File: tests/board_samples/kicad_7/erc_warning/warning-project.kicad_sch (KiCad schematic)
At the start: 0 parts

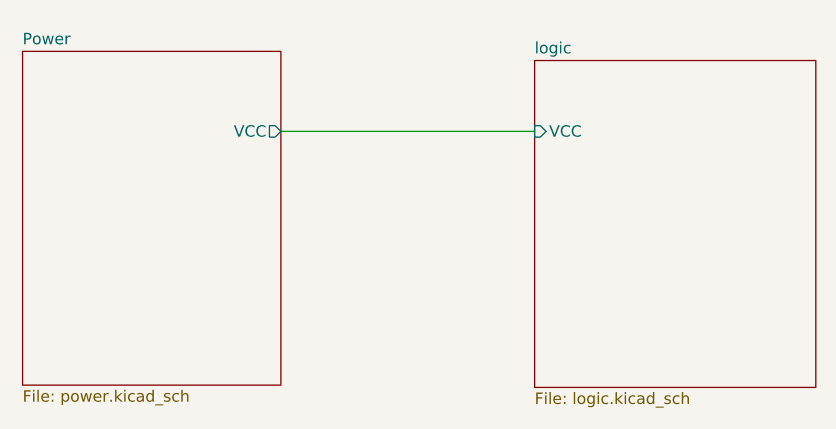
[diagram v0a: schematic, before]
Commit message: [Preflight][KiCad 7] Updated preflight references and tests
- Disabled PCB parity, API broken
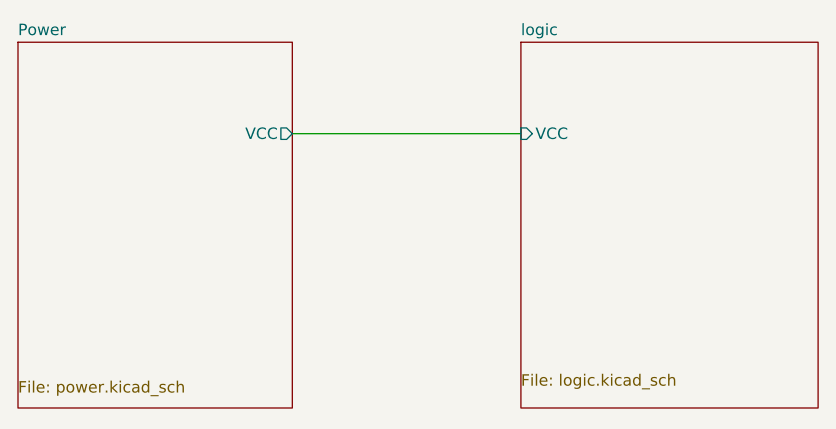
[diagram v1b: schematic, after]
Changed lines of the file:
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@@
 (kicad_sch (version 20230121) (generator eeschema)
   (paper "A4")
-  (wire (pts (xy 110.49 63.246) (xy 138.684 63.246))
-    (stroke (width 0) (type solid))
+  (wire (pts (xy 111.76 63.5) (xy 137.16 63.5))
+    (stroke (width 0) (type default))
   )
-  (sheet (at 81.788 54.356) (size 28.702 37.084)
+  (sheet (at 81.28 53.34) (size 30.48 40.64)
     (stroke (width 0) (type solid))
     (fill (color 0 0 0 0.0000))
-    (property "Sheetname" "Power" (at 81.788 53.7205 0)
+    (property "Sheetname" "Power" (at 81.28 52.7045 0)
       (effects (font (size 1.27 1.27)) (justify left bottom))
     )
-    (property "Sheetfile" "power.kicad_sch" (at 81.788 91.9485 0)
+    (property "Sheetfile" "power.kicad_sch" (at 81.28 90.9325 0)
       (effects (font (size 1.27 1.27)) (justify left top))
     )
-    (pin "VCC" output (at 110.49 63.246 0)
+    (pin "VCC" output (at 111.76 63.5 0)
       (effects (font (size 1.27 1.27)) (justify right))
     )
@@
     )
   )
-  (sheet (at 138.684 55.372) (size 31.242 36.322)
+  (sheet (at 137.16 53.34) (size 33.02 40.64)
     (stroke (width 0) (type solid))
     (fill (color 0 0 0 0.0000))
-    (property "Sheetname" "logic" (at 138.684 54.7365 0)
+    (property "Sheetname" "logic" (at 137.16 52.7045 0)
       (effects (font (size 1.27 1.27)) (justify left bottom))
     )
-    (property "Sheetfile" "logic.kicad_sch" (at 138.684 92.2025 0)
+    (property "Sheetfile" "logic.kicad_sch" (at 137.16 90.1705 0)
       (effects (font (size 1.27 1.27)) (justify left top))
     )
-    (pin "VCC" input (at 138.684 63.246 180)
+    (pin "VCC" input (at 137.16 63.5 180)
       (effects (font (size 1.27 1.27)) (justify left))
     )
